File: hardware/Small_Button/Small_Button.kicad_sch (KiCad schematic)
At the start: 5 parts, among them J1 JST PH, SW1 Cherry MX

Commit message: insert summary here
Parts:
- added H3: M2, MountingHole:MountingHole_2.2mm_M2_DIN965, symbol Mechanical:MountingHole
- added R1: 0R0, Resistor_SMD:R_0603_1608Metric, symbol Device:R_US
- J1: footprint Connector_JST:JST_SH_SM04B-SRSS-TB_1x04-1MP_P1.00mm_Horizontal -> Connector_JST:JST_SH_SM03B-SRSS-TB_1x03-1MP_P1.00mm_Horizontal; symbol Connector_Generic_MountingPin:Conn_01x04_MountingPin -> Connector_Generic_MountingPin:Conn_01x03_MountingPin; MPN (none) -> C160403
- SW1: now left out of the parts list
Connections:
- net GND: now also J1.3 (Pin_3), SW1.2, R1.2
- net LED+ renamed LED
- net LED-: no longer names the net of D1.1 (K)
- net LED-: now also R1.1; no longer J1.2 (Pin_2)
- net SW+ renamed SW
- net SW: now also J1.2 (Pin_2); no longer J1.3 (Pin_3)
- removed net SW-: J1.4 (Pin_4), SW1.2

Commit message: Update Small Button PCB
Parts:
- R1: value 0R0 -> 100Ω; MPN C15402 -> C25076
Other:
- company: (none) -> Geeks For Kids
- title: (none) -> Small Button PCB
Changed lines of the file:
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@@
 (kicad_sch
-	(version 20231120)
+	(version 20250114)
 	(generator "eeschema")
-	(generator_version "8.0")
+	(generator_version "9.0")
 	(paper "A4")
+	(title_block
+		(title "Small Button PCB")
+		(date "2025-04-13")
+		(rev "V1")
+		(company "Geeks For Kids")
+		(comment 1 "Learn Science and Math Club")
+	)
 	(junction
 		(at 106.68 102.87)
@@
 	(label "SW"
 		(at 132.08 90.17 0)
-		(fields_autoplaced yes)
 		(effects
 			(font
@@
 	(label "LED"
 		(at 132.08 100.33 0)
-		(fields_autoplaced yes)
 		(effects
 			(font
@@
 	(label "LED"
 		(at 121.92 91.44 180)
-		(fields_autoplaced yes)
 		(effects
 			(font
@@
 	(label "SW"
 		(at 121.92 93.98 180)
-		(fields_autoplaced yes)
 		(effects
 			(font
@@
 			)
 		)
-		(property "Value" "0R0"
+		(property "Value" "100Ω"
 			(at 156.21 96.52 90)
 			(effects
@@
 			)
 		)
-		(property "MPN" "C15402"
+		(property "MPN" "C25076"
 			(at 156.21 100.33 90)
 			(effects
@@
 		)
 	)
+	(embedded_fonts no)
 )

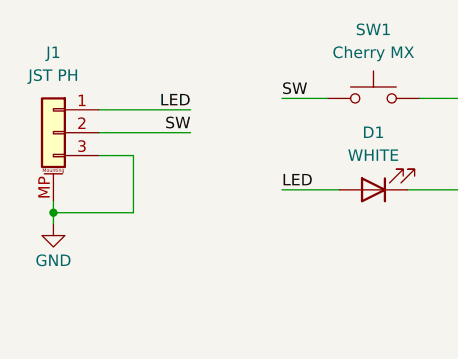
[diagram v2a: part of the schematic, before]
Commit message: Update Large Button PCB
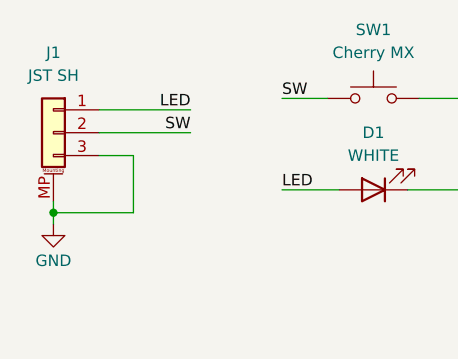
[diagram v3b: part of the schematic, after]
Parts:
- J1: value JST PH -> JST SH
- R1: footprint Resistor_SMD:R_0603_1608Metric -> Resistor_SMD:R_0402_1005Metric
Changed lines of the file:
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@@
 			)
 		)
-		(property "Footprint" "Resistor_SMD:R_0603_1608Metric"
+		(property "Footprint" "Resistor_SMD:R_0402_1005Metric"
 			(at 156.464 99.314 90)
 			(effects
@@
 			)
 		)
-		(property "Value" "JST PH"
+		(property "Value" "JST SH"
 			(at 106.68 87.63 0)
 			(effects

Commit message: update button pcb
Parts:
- R1: footprint Resistor_SMD:R_0402_1005Metric -> Resistor_SMD:R_0603_1608Metric; MPN C25076 -> C22775
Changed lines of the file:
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@@
 			)
 		)
-		(property "Footprint" "Resistor_SMD:R_0402_1005Metric"
+		(property "Footprint" "Resistor_SMD:R_0603_1608Metric"
 			(at 156.464 99.314 90)
 			(effects
@@
 			)
 		)
-		(property "MPN" "C25076"
+		(property "MPN" "C22775"
 			(at 156.21 100.33 90)
 			(effects

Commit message: Big commit
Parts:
- D1: now left out of the parts list
- R1: value 100Ω -> 150Ω; MPN C22775 -> C2907103
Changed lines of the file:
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@@
 			)
 		)
-		(property "Value" "100Ω"
+		(property "Value" "150Ω"
 			(at 156.21 96.52 90)
 			(effects
@@
 			)
 		)
-		(property "MPN" "C22775"
+		(property "MPN" "C2907103"
 			(at 156.21 100.33 90)
 			(effects
@@
 		(unit 1)
 		(exclude_from_sim no)
-		(in_bom yes)
-		(on_board yes)
-		(dnp no)
+		(in_bom no)
+		(on_board yes)
+		(dnp no)
